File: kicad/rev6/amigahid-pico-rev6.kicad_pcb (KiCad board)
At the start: 2 copper layers, 61.7 x 72.4 mm, 60 parts, among them J1 Amiga Keyboard, J2 Debug/programming, J3 i2c header, J4 USB_A, J5 Controller 1, J6 Controller 2, Q1 BSS138, Q10 BSS138, Q11 BSS138, Q12 BSS138, Q13 BSS138, Q14 BSS138, Q15 BSS138, Q16 BSS138, Q17 BSS138, Q2 BSS138, Q3 BSS138, Q4 BSS138, Q5 BSS138, Q6 BSS138, Q7 BSS138, Q8 BSS138, Q9 BSS138, U1 Pico

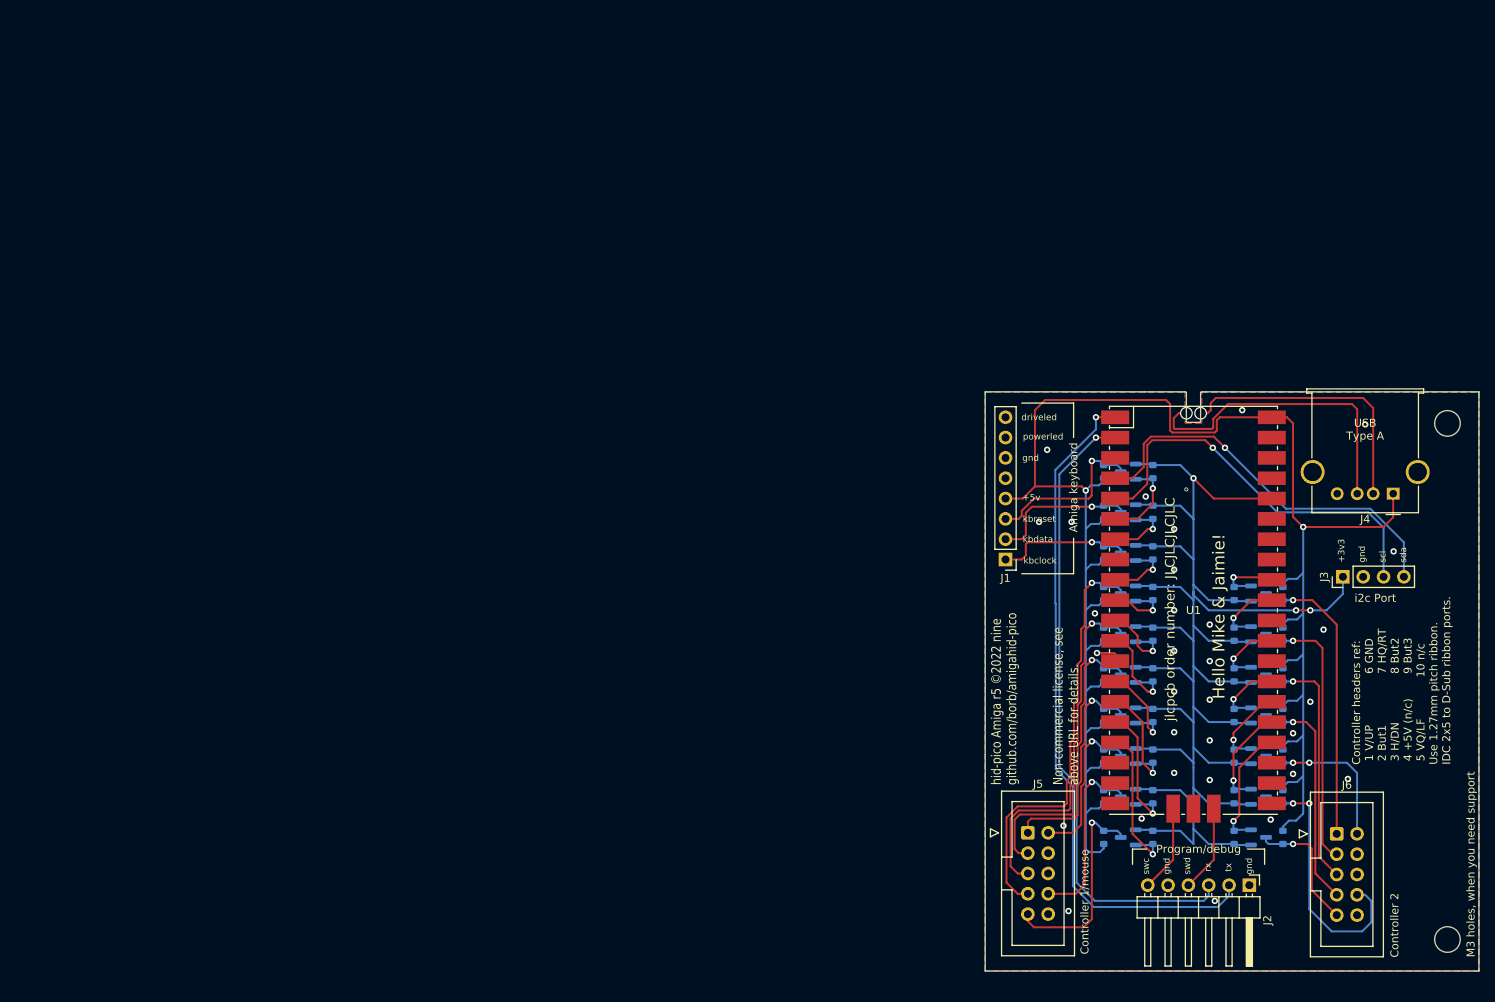
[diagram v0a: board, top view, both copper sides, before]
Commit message: kicad: rev6 board bootstrap - placement, outline, keepout
replace the copied rev5 board with a fresh rev6 layout built from the
rev6 schematic netlist. all 115 footprints placed with refdes, value,
LCSC/MPN fields and net-assigned pads; no tracks or pours yet.

100 x 80 mm, 2 layers, 3 mm rounded corners, 4x M3 NPTH at ~4 mm
corner offsets cut into Edge.Cuts.

  north  J9 DIN5-OUT / J10 mDIN6-OUT, gap, J11 DIN5-IN / J12 mDIN6-IN,
         20 mm between connector centres, mating faces flush north;
         J1 and J8 1x8 headers inboard of their groups
  south  P1 and P2 DE9 male, centres 24.0 and 76.6 mm (52.6 apart),
         hoods overhanging; J4 USB-A between them
  west   U1 antenna end flush with the edge; the west edge is the only
         free long edge that leaves the module's micro-usb pointing at
         open board, and it puts the kbd-out gpios (gp4-6) opposite the
         OUT connector group
  east   J13 USB-C aux 5V, D2, cc pulldowns - away from the antenna

U1 sits on top, rotated 270, with a >=15 mm corridor east of the
micro-usb clear of top-side parts for the flashing cable. board-level
rule area (F.Cu + B.Cu) over the antenna end, 11 x 15.8 mm, forbids
tracks, vias, pads and copper pour; footprints stay allowed there
because U1's own courtyard covers its antenna - the module's embedded
"antenna copper keep out" already rejects foreign footprints and pads.

19 BSS138 + 38 10k on the bottom in three regular grids: keyboard-out
north of the module, controller port 1 between the module's pad rows
(dodging the mid-board swd pads and the usb-tap slot), keyboard-in and
controller port 2 east of it. ESD clamps in rows under the connectors
they protect. F1/D1 at the AMIGA_5V entry, F3 and KBIN_5V decoupling by
J8, F2/C4/C5/U2 under J4, bulk C1 central on SYS5V.

silkscreen: TO AMIGA / FROM KEYBOARD over the two connector groups with
the one-amiga-at-a-time warning, module ANTENNA END / PIN 1 / USB
markers, port and led labels, the rev5 credit and non-comme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
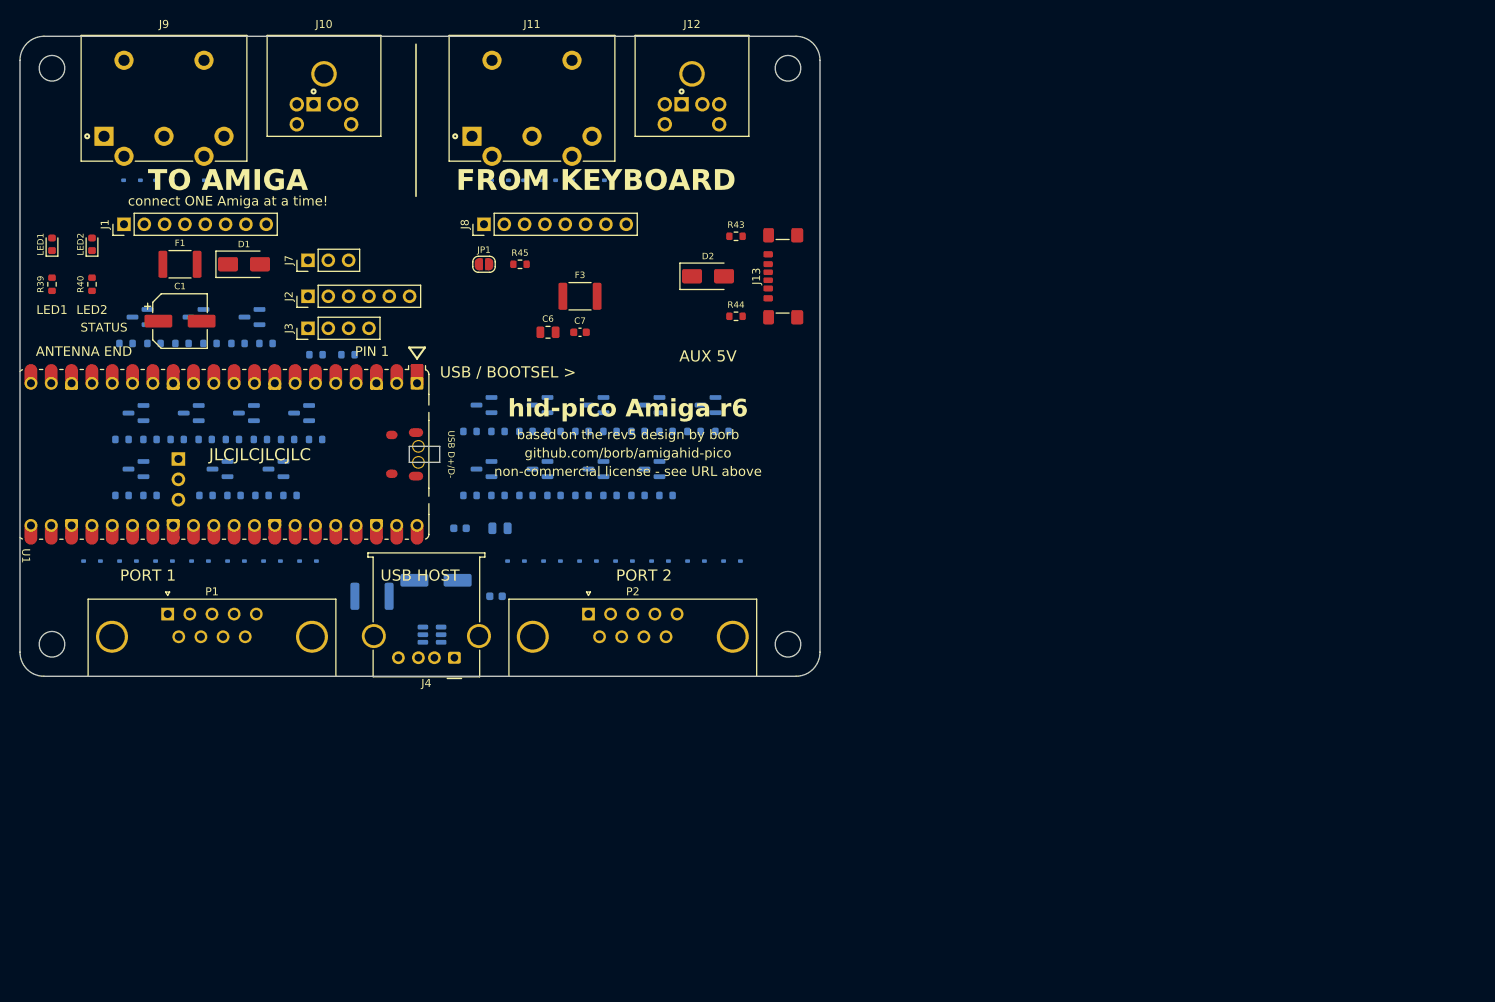
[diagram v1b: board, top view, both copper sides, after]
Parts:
- removed J5: Controller 1, Connector_IDC:IDC-Header_2x05_P2.54mm_Vertical
- removed J6: Controller 2, Connector_IDC:IDC-Header_2x05_P2.54mm_Vertical
- removed REF01, REF02: MountingHole_3.2mm_M3, MountingHole:MountingHole_3.2mm_M3
- removed locked: R1002, Resistor_SMD:R_0603_1608Metric
- added C1: 220uF, Capacitor_SMD:CP_Elec_6.3x7.7, F.Cu at (20.0, 35.6)
- added C2: 10uF, Capacitor_SMD:C_0805_2012Metric, B.Cu at (60.0, 61.5)
- added C3: 100nF, Capacitor_SMD:C_0603_1608Metric, B.Cu at (55.0, 61.5)
- added C4: 150uF, Capacitor_SMD:CP_Elec_6.3x7.7, B.Cu at (52.0, 68.0)
- added C5: 100nF, Capacitor_SMD:C_0603_1608Metric, B.Cu at (59.5, 70.0)
- added C6: 10uF, Capacitor_SMD:C_0805_2012Metric, F.Cu at (66.0, 37.0)
- added C7: 100nF, Capacitor_SMD:C_0603_1608Metric, F.Cu at (70.0, 37.0)
- added D1: SS34, Diode_SMD:D_SMA, F.Cu at (28.0, 28.5)
- added D10: PESD5V0S1BA, Diode_SMD:D_SOD-323, B.Cu at (14.0, 18.0)
- added D11: PESD5V0S1BA, Diode_SMD:D_SOD-323, B.Cu at (18.0, 18.0)
- added D12: PESD5V0S1BA, Diode_SMD:D_SOD-323, B.Cu at (22.0, 18.0)
- added D13: PESD5V0S1BA, Diode_SMD:D_SOD-323, B.Cu at (9.00, 65.6)
- added D14: PESD5V0S1BA, Diode_SMD:D_SOD-323, B.Cu at (13.5, 65.6)
- added D15: PESD5V0S1BA, Diode_SMD:D_SOD-323, B.Cu at (18.0, 65.6)
- added D16: PESD5V0S1BA, Diode_SMD:D_SOD-323, B.Cu at (22.5, 65.6)
- added D17: PESD5V0S1BA, Diode_SMD:D_SOD-323, B.Cu at (27.0, 65.6)
- added D18: PESD5V0S1BA, Diode_SMD:D_SOD-323, B.Cu at (31.5, 65.6)
- added D19: PESD5V0S1BA, Diode_SMD:D_SOD-323, B.Cu at (36.0, 65.6)
- added D2: SS34, Diode_SMD:D_SMA, F.Cu at (86.0, 30.0)
- added D20: PESD5V0S1BA, Diode_SMD:D_SOD-323, B.Cu at (60.0, 18.0)
- added D21: PESD5V0S1BA, Diode_SMD:D_SOD-323, B.Cu at (64.0, 18.0)
- added D22: PESD5V0S1BA, Diode_SMD:D_SOD-323, B.Cu at (62.0, 65.6)
- added D23: PESD5V0S1BA, Diode_SMD:D_SOD-323, B.Cu at (66.5, 65.6)
- added D24: PESD5V0S1BA, Diode_SMD:D_SOD-323, B.Cu at (71.0, 65.6)
- added D25: PESD5V0S1BA, Diode_SMD:D_SOD-323, B.Cu at (75.5, 65.6)
- added D26: PESD5V0S1BA, Diode_SMD:D_SOD-323, B.Cu at (80.0, 65.6)
- added D27: PESD5V0S1BA, Diode_SMD:D_SOD-323, B.Cu at (84.5, 65.6)
- added D28: PESD5V0S1BA, Diode_SMD:D_SOD-323, B.Cu at (89.0, 65.6)
- added D29: PESD5V0S1BA, Diode_SMD:D_SOD-323, B.Cu at (68.0, 18.0)
- added D30: PESD5V0S1BA, Diode_SMD:D_SOD-323, B.Cu at (72.0, 18.0)
- added F1: 750mA, Fuse:Fuse_1812_4532Metric, F.Cu at (20.0, 28.5)
- added F2: 500mA, Fuse:Fuse_1812_4532Metric, B.Cu at (44.0, 70.0)
- added F3: 500mA, Fuse:Fuse_1812_4532Metric, F.Cu at (70.0, 32.5)
- added J10: PS/2 KBD OUT, rev6:MiniDIN6_PS2_Socket_CUI_MD-60S, F.Cu at (38.0, 0.00)
- added J11: DIN5 KBD IN, rev6:DIN5_180deg_Socket_Kycon_KCDX-5S-N, F.Cu at (64.0, 0.00)
- added J12: PS/2 KBD IN, rev6:MiniDIN6_PS2_Socket_CUI_MD-60S, F.Cu at (84.0, 0.00)
- added J13: USB-C AUX 5V, Connector_USB:USB_C_Receptacle_GCT_USB4135-GF-A_6P_TopMnt_Horizontal, F.Cu at (96.5, 30.0)
- added J7: SPARE GP28, Connector_PinHeader_2.54mm:PinHeader_1x03_P2.54mm_Vertical, F.Cu at (36.0, 28.0)
- added J8: A500 KBD IN, Connector_PinHeader_2.54mm:PinHeader_1x08_P2.54mm_Vertical, F.Cu at (58.0, 23.5)
- added J9: DIN5 KBD OUT, rev6:DIN5_180deg_Socket_Kycon_KCDX-5S-N, F.Cu at (18.0, 0.00)
- added JP1: KBIN PWRLED, Jumper:SolderJumper-2_P1.3mm_Open_RoundedPad1.0x1.5mm, F.Cu at (58.0, 28.5)
- added LED1: red, LED_SMD:LED_0603_1608Metric, F.Cu at (4.00, 26.0)
- added LED2: yellow-green, LED_SMD:LED_0603_1608Metric, F.Cu at (9.00, 26.0)
- added P1: DE9 MALE PORT 1, Connector_Dsub:DSUB-9_Pins_Horizontal_P2.77x2.84mm_EdgePinOffset4.94mm_Housed_MountingHolesOffset4.94mm, F.Cu at (18.5, 72.2)
- added P2: DE9 MALE PORT 2, Connector_Dsub:DSUB-9_Pins_Horizontal_P2.77x2.84mm_EdgePinOffset4.94mm_Housed_MountingHolesOffset4.94mm, F.Cu at (71.1, 72.2)
- added Q18: BSS138, Package_TO_SOT_SMD:SOT-23, B.Cu at (72.0, 54.1)
- added Q19: BSS138, Package_TO_SOT_SMD:SOT-23, B.Cu at (79.0, 54.1)
- added R15: 10k, Resistor_SMD:R_0603_1608Metric, B.Cu at (12.8, 57.4)
- added R35: 10k, Resistor_SMD:R_0603_1608Metric, B.Cu at (70.2, 57.4)
- added R36: 10k, Resistor_SMD:R_0603_1608Metric, B.Cu at (73.8, 57.4)
- added R37: 10k, Resistor_SMD:R_0603_1608Metric, B.Cu at (77.2, 57.4)
- added R38: 10k, Resistor_SMD:R_0603_1608Metric, B.Cu at (80.8, 57.4)
- added R39: 1k, Resistor_SMD:R_0603_1608Metric, F.Cu at (4.00, 31.0)
- added R40: 1k, Resistor_SMD:R_0603_1608Metric, F.Cu at (9.00, 31.0)
- added R41: 4.7k, Resistor_SMD:R_0603_1608Metric, B.Cu at (37.0, 39.8)
- added R42: 4.7k, Resistor_SMD:R_0603_1608Metric, B.Cu at (41.0, 39.8)
- added R43: 5.1k, Resistor_SMD:R_0603_1608Metric, F.Cu at (89.5, 25.0)
- added R44: 5.1k, Resistor_SMD:R_0603_1608Metric, F.Cu at (89.5, 35.0)
- added R45: 470, Resistor_SMD:R_0603_1608Metric, F.Cu at (62.5, 28.5)
- added U2: USBLC6-2SC6, Package_TO_SOT_SMD:SOT-23-6, B.Cu at (51.5, 74.8)
- J1: value Amiga Keyboard -> A500 KBD OUT
- J2: value Debug/programming -> DEBUG UART+SWD; footprint Connector_PinHeader_2.54mm:PinHeader_1x06_P2.54mm_Horizontal -> Connector_PinHeader_2.54mm:PinHeader_1x06_P2.54mm_Vertical
- J3: value i2c header -> OLED I2C
- J4: value USB_A -> USB-A HOST
- R1, R10, R11, R12, R13, R14, R16, R17, R18, R19, R2, R20, R21, R22, R23, R24, R25, R26, R27, R28, R29, R3, R30, R31, R32, R33, R34, R4, R5, R6, R7, R8, R9: value R1002 -> 10k
- U1: value Pico -> PicoW; footprint MCU_RaspberryPi_and_Boards:RPi_Pico_SMD_TH -> rev6:RPi_PicoW_SMD_TH
- moved J2 138.8 mm to (36.0, 32.5), turned to 90 degrees
- moved J3 133.0 mm to (36.0, 36.5)
- moved R16 129.5 mm to (16.2, 57.4), turned to 180 degrees
- moved Q8 129.1 mm to (14.5, 54.1)
- moved R8 126.8 mm to (16.2, 50.4), turned to 180 degrees
- moved Q4 126.1 mm to (14.5, 47.1)
- moved R6 125.9 mm to (16.8, 38.4), turned to 180 degrees
- moved Q3 125.0 mm to (15.0, 35.1)
- moved R7 124.2 mm to (12.8, 50.4), turned to 180 degrees
- moved R5 123.3 mm to (13.2, 38.4), turned to 180 degrees
- moved U1 122.7 mm to (25.5, 52.3), turned to -90 degrees
- moved R10 120.9 mm to (23.1, 50.4), turned to 180 degrees
- moved R18 120.9 mm to (26.8, 57.4), turned to 180 degrees
- moved Q9 120.7 mm to (25.0, 54.1)
- moved Q5 120.3 mm to (21.4, 47.1)
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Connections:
- net /i2c scl renamed /i2c_scl
- net /i2c sda renamed /i2c_sda
- net /uart rx renamed /uart_rx
- net /uart tx renamed /uart_tx
- J1 pad 4: +5V -> /AMIGA_5V
- J1 pad 5: unconnected-(J1-Pad5) -> (no net)
- J1 pad 7: /kbpowerled -> /kb_pwrled
- J1 pad 8: /kbdriveled -> /kb_drvled
- J4 pad 1: +5V -> /USBA_5V
- J4 pad 2: /usb d- -> /usb_dm
- J4 pad 3: /usb d+ -> /usb_dp
- Q1 pad 2: /lkbclock -> /kbreset_lo
- Q1 pad 3: /kbclock -> /kbreset
- Q10 pad 2: /lcont1 b3 -> /cont1_b3_lo
- Q10 pad 3: /cont1 b3 -> /cont1_b3
- Q11 pad 2: /lcont2 v -> /kbin_clk_lo
- Q11 pad 3: /cont2 v -> /kbin_clk
- Q12 pad 2: /lcont2 h -> /kbin_dat_lo
- Q12 pad 3: /cont2 h -> /kbin_dat
- Q13 pad 2: /lcont2 vq -> /cont2_b3_lo
- Q13 pad 3: /cont2 vq -> /cont2_b3
- Q14 pad 2: /lcont2 hq -> /cont2_b2_lo
- Q14 pad 3: /cont2 hq -> /cont2_b2
- Q15 pad 2: /lcont2 b1 -> /cont2_b1_lo
- Q15 pad 3: /cont2 b1 -> /cont2_b1
- Q16 pad 2: /lcont2 b2 -> /cont2_hq_lo
- Q16 pad 3: /cont2 b2 -> /cont2_hq
- Q17 pad 2: /lcont2 b3 -> /cont2_vq_lo
- Q17 pad 3: /cont2 b3 -> /cont2_vq
- Q2 pad 2: /lkbdata -> /kbdata_lo
- Q3 pad 2: /lkbreset -> /kbclock_lo
- Q3 pad 3: /kbreset -> /kbclock
- Q4 pad 2: /lcont1 hq -> /cont1_hq_lo
- Q4 pad 3: /cont1 hq -> /cont1_hq
- Q5 pad 2: /lcont1 vq -> /cont1_vq_lo
- Q5 pad 3: /cont1 vq -> /cont1_vq
- Q6 pad 2: /lcont1 h -> /cont1_h_lo
- Q6 pad 3: /cont1 h -> /cont1_h
- Q7 pad 2: /lcont1 v -> /cont1_v_lo
- Q7 pad 3: /cont1 v -> /cont1_v
- Q8 pad 2: /lcont1 b1 -> /cont1_b1_lo
- Q8 pad 3: /cont1 b1 -> /cont1_b1
- Q9 pad 2: /lcont1 b2 -> /cont1_b2_lo
- Q9 pad 3: /cont1 b2 -> /cont1_b2
- R1 pad 1: /kbclock -> +3V3
- R1 pad 2: +5V -> /kbreset_lo
- R10 pad 1: /lcont1 vq -> /SYS5V
- R10 pad 2: +3V3 -> /cont1_vq
- R11 pad 1: /cont1 h -> +3V3
- R11 pad 2: +5V -> /cont1_h_lo
- R12 pad 1: /lcont1 h -> /SYS5V
- R12 pad 2: +3V3 -> /cont1_h
- R13 pad 1: /cont1 v -> +3V3
- R13 pad 2: +5V -> /cont1_v_lo
- R14 pad 1: /lcont1 v -> /SYS5V
- R14 pad 2: +3V3 -> /cont1_v
- R16 pad 1: /lcont1 b1 -> /SYS5V
- R16 pad 2: +3V3 -> /cont1_b1
- R17 pad 1: /cont1 b2 -> +3V3
- R17 pad 2: +5V -> /cont1_b2_lo
- R18 pad 1: /lcont1 b2 -> /SYS5V
- R18 pad 2: +3V3 -> /cont1_b2
- R19 pad 1: /cont1 b3 -> +3V3
- R19 pad 2: +5V -> /cont1_b3_lo
- R2 pad 1: /lkbclock -> /SYS5V
- R2 pad 2: +3V3 -> /kbreset
- R20 pad 1: /lcont1 b3 -> /SYS5V
- R20 pad 2: +3V3 -> /cont1_b3
- R21 pad 1: /cont2 v -> +3V3
- R21 pad 2: +5V -> /kbin_clk_lo
- R22 pad 1: /lcont2 v -> /SYS5V
- R22 pad 2: +3V3 -> /kbin_clk
- R23 pad 1: /cont2 h -> +3V3
- R23 pad 2: +5V -> /kbin_dat_lo
- R24 pad 1: /lcont2 h -> /SYS5V
- R24 pad 2: +3V3 -> /kbin_dat
- R25 pad 1: /cont2 vq -> +3V3
- R25 pad 2: +5V -> /cont2_b3_lo
- R26 pad 1: /lcont2 vq -> /SYS5V
- R26 pad 2: +3V3 -> /cont2_b3
- R27 pad 1: /cont2 hq -> +3V3
- R27 pad 2: +5V -> /cont2_b2_lo
- R28 pad 1: /lcont2 hq -> /SYS5V
- R28 pad 2: +3V3 -> /cont2_b2
- R29 pad 1: /cont2 b1 -> +3V3
- R29 pad 2: +5V -> /cont2_b1_lo
- R3 pad 1: /kbdata -> +3V3
- R3 pad 2: +5V -> /kbdata_lo
- R30 pad 1: /lcont2 b1 -> /SYS5V
- R30 pad 2: +3V3 -> /cont2_b1
- R31 pad 1: /cont2 b2 -> +3V3
- R31 pad 2: +5V -> /cont2_hq_lo
- R32 pad 1: /lcont2 b2 -> /SYS5V
- R32 pad 2: +3V3 -> /cont2_hq
- R33 pad 1: /cont2 b3 -> +3V3
- R33 pad 2: +5V -> /cont2_vq_lo
- R34 pad 1: /lcont2 b3 -> /SYS5V
- R34 pad 2: +3V3 -> /cont2_vq
- R4 pad 1: /lkbdata -> /SYS5V
- R4 pad 2: +3V3 -> /kbdata
- R5 pad 1: /kbreset -> +3V3
- R5 pad 2: +5V -> /kbclock_lo
- R6 pad 1: /lkbreset -> /SYS5V
- R6 pad 2: +3V3 -> /kbclock
- R7 pad 1: /cont1 hq -> +3V3
- R7 pad 2: +5V -> /cont1_hq_lo
- R8 pad 1: /lcont1 hq -> /SYS5V
- R8 pad 2: +3V3 -> /cont1_hq
- R9 pad 1: /cont1 vq -> +3V3
- R9 pad 2: +5V -> /cont1_vq_lo
- U1 pad 10: /lcont1 hq -> /cont1_hq_lo
- U1 pad 11: /lcont1 vq -> /cont1_vq_lo
- U1 pad 12: /lcont1 h -> /cont1_h_lo
- U1 pad 14: /lcont1 v -> /cont1_v_lo
- U1 pad 15: /lcont1 b1 -> /cont1_b1_lo
- U1 pad 16: /lcont1 b2 -> /cont1_b2_lo
- U1 pad 17: /lcont1 b3 -> /cont1_b3_lo
- U1 pad 19: unconnected-(U1-Pad19) -> /kbin_clk_lo
- U1 pad 20: unconnected-(U1-Pad20) -> /kbin_dat_lo
- U1 pad 21: unconnected-(U1-Pad21) -> /led1_drv
- U1 pad 22: unconnected-(U1-Pad22) -> /led2_drv
- U1 pad 24: /lcont2 b3 -> /cont2_b3_lo
- U1 pad 25: /lcont2 b2 -> /cont2_b2_lo
- U1 pad 26: /lcont2 b1 -> /cont2_b1_lo
- U1 pad 27: /lcont2 hq -> /cont2_hq_lo
- U1 pad 29: /lcont2 vq -> /cont2_vq_lo
- U1 pad 30: unconnected-(U1-Pad30) -> (no net)
- U1 pad 31: /lcont2 h -> /cont2_h_lo
- U1 pad 32: /lcont2 v -> /cont2_v_lo
- U1 pad 34: unconnected-(U1-Pad34) -> /gp28
- U1 pad 35: unconnected-(U1-Pad35) -> (no net)
- U1 pad 37: unconnected-(U1-Pad37) -> (no net)
- U1 pad 39: unconnected-(U1-Pad39) -> /SYS5V
- U1 pad 40: +5V -> (no net)
- U1 pad 6: /lkbreset -> /kbreset_lo
- U1 pad 7: /lkbdata -> /kbdata_lo
- U1 pad 9: /lkbclock -> /kbclock_lo
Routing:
- net +5V: track 220.3 -> 0.00 mm, vias 2 -> 0
- net +3V3: track 213.8 -> 0.00 mm, vias 3 -> 0
- net /uart_tx: track 87.4 -> 0.00 mm, vias 1 -> 0
- net /uart_rx: track 80.8 -> 0.00 mm, vias 1 -> 0
- net /cont1 hq: track 52.9 -> 0.00 mm, vias 1 -> 0
- net /i2c_scl: track 49.2 -> 0.00 mm, vias 1 -> 0
- net /i2c_sda: track 48.8 -> 0.00 mm, vias 1 -> 0
- net /cont1 vq: track 45.1 -> 0.00 mm, vias 1 -> 0
- net /usb d+: track 39.1 -> 0.00 mm, vias 1 -> 0
- net /cont1 h: track 38.1 -> 0.00 mm, vias 1 -> 0
- net /cont2 v: track 36.9 -> 0.00 mm, vias 1 -> 0
- net /cont2 h: track 34.9 -> 0.00 mm, vias 1 -> 0
- net /usb d-: track 33.9 -> 0.00 mm, vias 1 -> 0
- net /cont2 b2: track 33.4 -> 0.00 mm, vias 2 -> 0
- net /cont2 vq: track 32.0 -> 0.00 mm, vias 1 -> 0
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- removed copper zone on B.Cu, net GND
- removed copper zone on F.Cu, net GND
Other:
- board size 61.7 x 72.4 mm -> 100 x 80 mm
- board text added: "ANTENNA END"
- board text added: "AUX 5V"
- board text added: "FROM KEYBOARD"
- board text added: "JLCJLCJLCJLC"
- board text added: "LED1"
- board text added: "LED2"
- board text added: "PIN 1"
- board text added: "PORT 1"
- board text added: "PORT 2"
- board text added: "STATUS"
- board text added: "TO AMIGA"
- board text added: "USB / BOOTSEL >"
- board text added: "USB HOST"
- board text added: "based on the rev5 design by borb"
- board text added: "connect ONE Amiga at a time!"
- board text added: "github.com/borb/amigahid-pico"
- board text added: "hid-pico Amiga r6"
- board text added: "non-commercial license - see URL above"
- board text removed: "+3v3 gnd scl sda"
- board text removed: "+5v"
- board text removed: "6 GND 7 HQ/RT 8 But2 9 But3 10 n/c"
- board text removed: "All FETs (Q*) part BSS138 All resistors (R*) part R1002"
- board text removed: "Amiga keyboard"
- board text removed: "Controller 1/mouse"
- board text removed: "Controller 2"
- board text removed: "Controller headers ref: 1 V/UP 2 But1 3 H/DN 4 +5V (n/c) 5 VQ/LF Use 1.27mm pitch ribbon. IDC 2x5 to D-Sub ribbon ports."
- board text removed: "Hello Mike & Jaimie!"
- board text removed: "M3 holes, when you need support"
- board text removed: "Program/debug"
- board text removed: "Solder VERY carefully to --> enable USB Type A port. Pico test pads are very close to shield (ground) solder points."
- board text removed: "USB Type A"
- board text removed: "driveled"
- board text removed: "gnd"
- board text removed: "hid-pico Amiga r5 ©️2022 nine github.com/borb/amigahid-pico Non-commercial license, see above URL for details."
- board text removed: "i2c Port"
- board text removed: "jlcpcb order number: JLCJLCJLCJLC"
- board text removed: "kbclock"
- board text removed: "kbdata"
- board text removed: "kbreset"
- board text removed: "powerled"
- board text removed: "swc gnd swd rx tx gnd"

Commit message: kicad: fix rev6 placement ahead of routing
J4 was fitted back to front: the Molex 67643 land pattern mates at its
local +y, so the receptacle was pointing into the board and its pads sat
2.8 mm from the south edge instead of 13.5 mm.  Turned round and pushed
out, which also brings the USB tap within reach - usb_dp/usb_dm could not
have been routed under 25 mm the way it stood.

Other placement work:

  - U1 1 mm north, opening a component band between the module and J4;
    R7..R14 follow so the SWD pads keep clear of R9.
  - U2 (USBLC6) and F2 to the top side as the layout brief requires, U2
    turned 90 deg so each USB line runs straight down one pad column
    from the tap to the connector.  C4 follows.
  - TP2/TP3 declared castellated pads: they are half vias deliberately
    bisected by the milled USB-tap window, as on rev 5, and that is what
    the pad property is for.
  - antenna rule area grown to the full 11 x 15.8 mm guarded region and
    set to forbid footprints as well as copper.
  - silkscreen trimmed back inside the board outline (edge connectors
    were printing past it) and the labels that landed on J4/U2 moved.
  - the edited footprints are vendored into rev6.pretty so the board no
    longer differs from its libraries; U1's six unnamed editing groups
    are dropped, and the zone points FootprintSave writes are corrected
    (it rotates footprint rule areas into the library frame but does not
    translate them).
  - the JP1/R45 link gets a name, kb_pwrled_bal, so schematic parity has
    something to match.

DRC is clean bar the 291 unrouted connections; netlist checker 356/356.
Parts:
- F2, U2: moved to F.Cu
- J4: footprint Connector_USB:USB_A_Molex_67643_Horizontal -> rev6:USB_A_Molex_67643_Horizontal
- P1, P2: footprint Connector_Dsub:DSUB-9_Pins_Horizontal_P2.77x2.84mm_EdgePinOffset4.94mm_Housed_MountingHolesOffset4.94mm -> rev6:DSUB-9_Pins_Horizontal_P2.77x2.84mm_EdgePinOffset4.94mm_Housed_MountingHolesOffset4.94mm
- moved J4 9.68 mm to (47.3, 71.0), turned to 0 degrees
- moved U2 9.33 mm to (50.8, 65.5), turned to 90 degrees
- moved F2 9.13 mm to (36.0, 65.6), turned to 0 degrees
- moved C4 2.56 mm to (50.4, 66.0)
- moved U1 1.00 mm to (25.5, 51.3)
- moved R10 0.30 mm to (23.1, 50.1)
- moved R11 0.30 mm to (26.6, 50.1)
- moved R12 0.30 mm to (30.1, 50.1)
- moved R13 0.30 mm to (33.5, 50.1)
- moved R14 0.30 mm to (37.0, 50.1)
- moved R7 0.30 mm to (12.8, 50.1)
- moved R8 0.30 mm to (16.2, 50.1)
- moved R9 0.30 mm to (19.6, 50.1)
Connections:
- net Net-(JP1-B) renamed /kb_pwrled_bal
